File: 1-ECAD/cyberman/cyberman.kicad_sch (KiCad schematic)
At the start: 0 parts

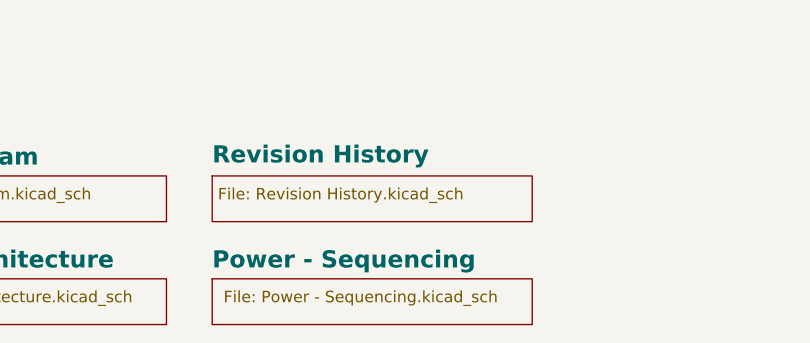
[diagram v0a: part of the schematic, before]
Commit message: esp32 supply
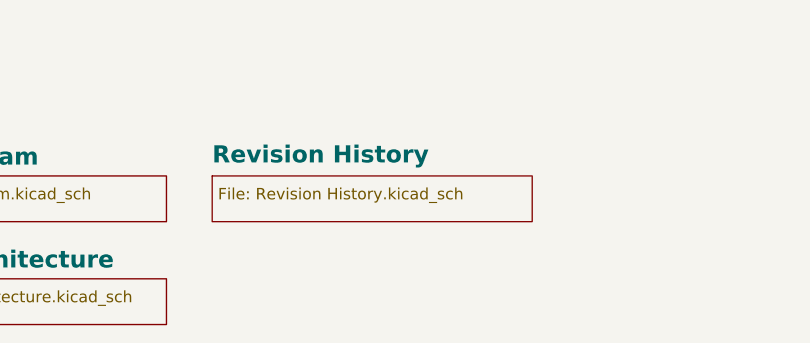
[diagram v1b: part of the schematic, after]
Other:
- removed sheet Power - Sequencing
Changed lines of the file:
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@@
 		(effects
 			(font
-				(face "Arial")
+				(face "Times New Roman")
 				(size 2 2)
 				(color 0 0 0 1)
@@
 		(effects
 			(font
-				(face "Arial")
+				(face "Times New Roman")
 				(size 2 2)
 				(thickness 0.4)
@@
 		(effects
 			(font
-				(face "Arial")
+				(face "Times New Roman")
 				(size 2 2)
 				(color 0 0 0 1)
@@
 		(effects
 			(font
-				(face "Arial")
+				(face "Times New Roman")
 				(size 2 2)
 				(color 0 0 0 1)
@@
 		(effects
 			(font
-				(face "Arial")
+				(face "Times New Roman")
 				(size 2 2)
 				(thickness 0.4)
@@
 		(effects
 			(font
-				(face "Arial")
+				(face "Times New Roman")
 				(size 5 5)
 				(bold yes)
@@
 		(effects
 			(font
-				(face "Arial")
+				(face "Times New Roman")
 				(size 5 5)
 				(bold yes)
@@
 		(effects
 			(font
-				(face "Arial")
+				(face "Times New Roman")
 				(size 5 5)
 				(bold yes)
@@
 		(effects
 			(font
-				(face "Arial")
+				(face "Times New Roman")
 				(size 5 5)
 				(bold yes)
@@
 		)
 	)
-	(sheet
-		(at 340.36 313.69)
-		(size 35.56 5.08)
-		(stroke
-			(width 0.1524)
-			(type solid)
-		)
-		(fill
-			(color 0 0 0 0.0000)
-		)
-		(property "Sheetname" "Power - Sequencing"
-			(at 340.36 312.6609 0)
-			(effects
-				(font
-					(face "Times New Roman")
-					(size 1.905 1.905)
-					(bold yes)
-					(color 0 0 0 1)
-				)
-				(justify left bottom)
-			)
-		)
-		(property "Sheetfile" "Power - Sequencing.kicad_sch"
-			(at 341.63 314.96 0)
-			(effects
-				(font
-					(face "Arial")
-					(size 1.27 1.27)
-				)
-				(justify left top)
-			)
-		)
-		(instances
-			(project "cyberman"
-				(path "/0650c7a8-acba-429c-9f8e-eec0baf0bc1c"
-					(page "6")
-				)
-			)
-		)
-	)

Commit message: update power sche
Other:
- note added: "MCU - IOs"
- note added: "MCU - Power"
- note removed: "Random Sheet 1"
- note removed: "Random Sheet 2"
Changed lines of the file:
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@@
 		)
 	)
-	(text "Random Sheet 1"
+	(text "MCU - Power"
 		(exclude_from_sim no)
 		(at 45.72 106.68 0)
@@
 		)
 	)
-	(text "Random Sheet 2"
+	(text "MCU - IOs"
 		(exclude_from_sim no)
 		(at 45.72 114.3 0)

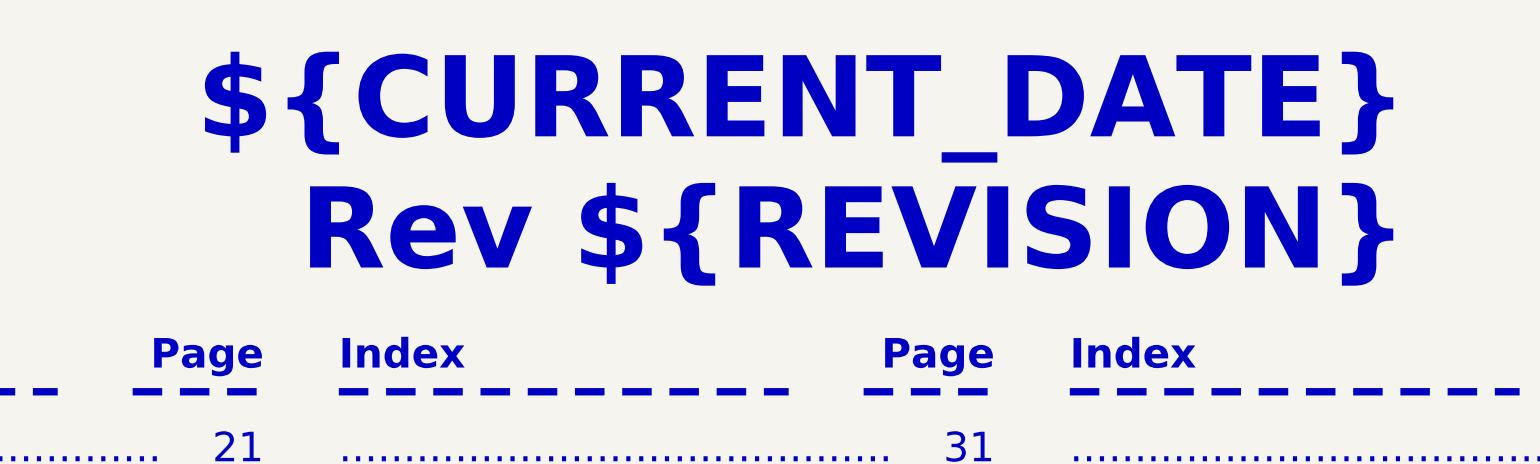
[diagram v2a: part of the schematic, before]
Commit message: new changes
close display page and peripheral schematic
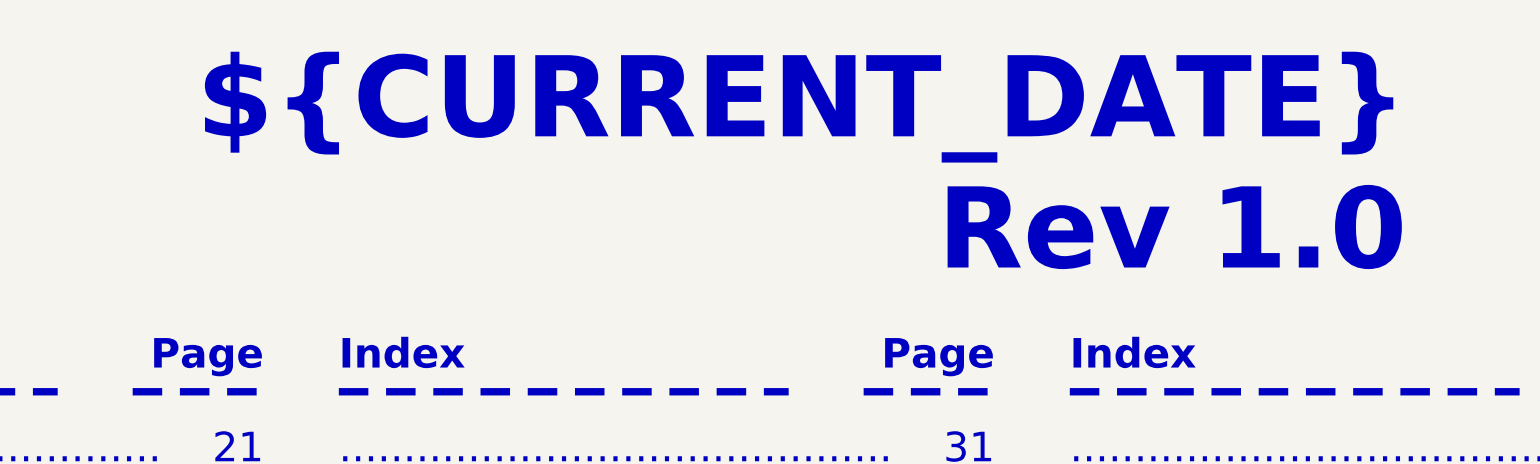
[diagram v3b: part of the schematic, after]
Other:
- company: ${COMPANY} -> kode.
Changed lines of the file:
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@@
 	(title_block
 		(title "Cover Page")
-		(date "Last Modified Date")
-		(rev "${REVISION}")
-		(company "${COMPANY}")
+		(date "2024-12-11")
+		(rev "1.0")
+		(company "kode.")
 	)
 	(polyline
